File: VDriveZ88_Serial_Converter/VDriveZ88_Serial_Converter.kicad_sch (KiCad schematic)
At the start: 12 parts, among them J1 VDrive, J2 Z88, J3 Power, U1 MAX232

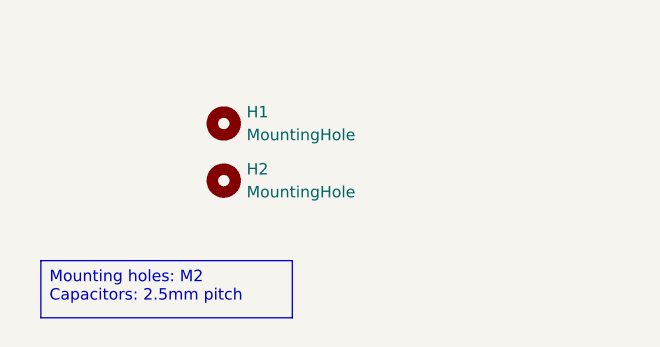
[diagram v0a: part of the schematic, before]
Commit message: Changed VDrive connector to 2mm pitch
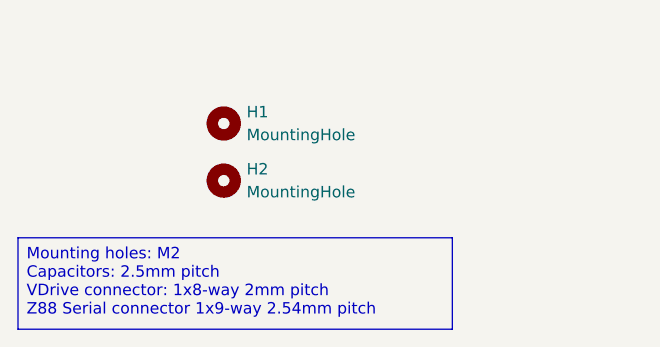
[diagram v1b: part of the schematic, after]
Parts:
- J1: footprint Connector_PinHeader_2.54mm:PinHeader_1x08_P2.54mm_Vertical -> Connector_PinHeader_2.00mm:PinHeader_1x08_P2.00mm_Vertical
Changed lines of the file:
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@@
 		(company "Brett Hallen")
 	)
-	(text_box "Mounting holes: M2\nCapacitors: 2.5mm pitch"
+	(text_box "Mounting holes: M2\nCapacitors: 2.5mm pitch\nVDrive connector: 1x8-way 2mm pitch\nZ88 Serial connector 1x9-way 2.54mm pitch"
 		(exclude_from_sim no)
-		(at 16.51 125.73 0)
-		(size 27.94 6.35)
+		(at 13.97 123.19 0)
+		(size 48.26 10.16)
 		(margins 0.9525 0.9525 0.9525 0.9525)
 		(stroke
@@
 			)
 		)
-		(property "Footprint" "Connector_PinHeader_2.54mm:PinHeader_1x08_P2.54mm_Vertical"
+		(property "Footprint" "Connector_PinHeader_2.00mm:PinHeader_1x08_P2.00mm_Vertical"
 			(at 114.3 27.94 0)
 			(effects
